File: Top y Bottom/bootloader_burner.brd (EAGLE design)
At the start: 57 x 53.3 mm, 9 parts, among them J1 ZIFSOCKET-28-3", Y1 16MHz

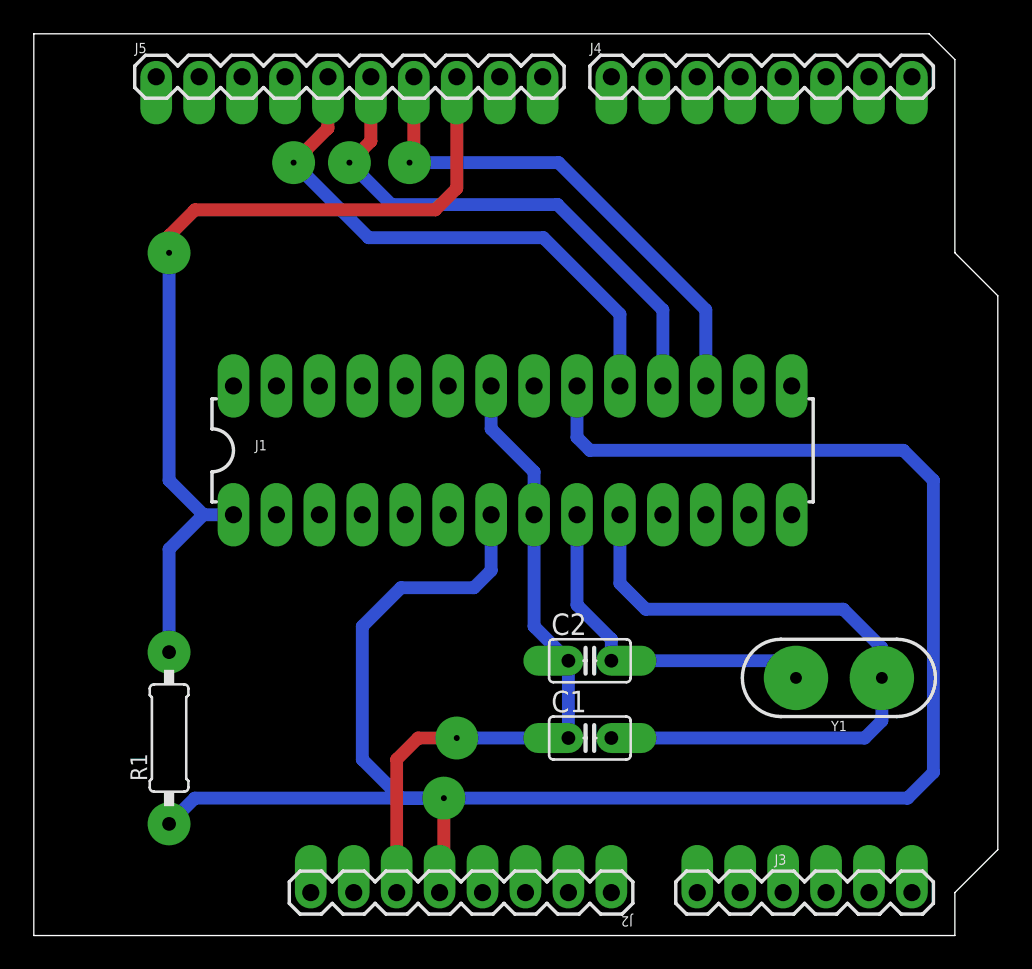
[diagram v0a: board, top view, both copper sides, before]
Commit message: Cambie el diseño de la plaqueta con zif socket grande para que queden ordenados los pines con los del Arduino. Tambien cambie el dieño de la plaqueta doble (que igual hay que cambiarla poque la gracia de esa es que quede montada en el Arduino)
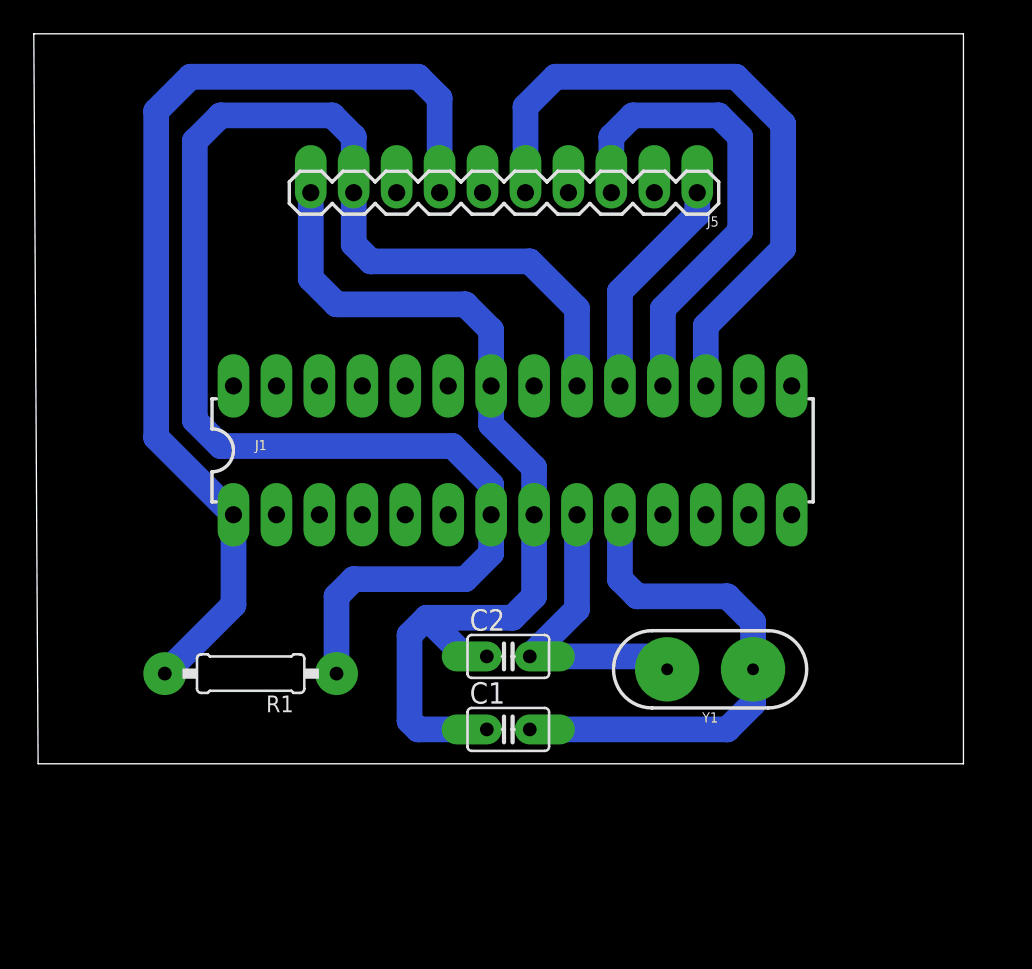
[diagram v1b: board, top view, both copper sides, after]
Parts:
- removed J2, J4: (no value), SparkFun-Connectors:1X08
- removed J3: (no value), SparkFun-Connectors:1X06
- moved J5 32.7 mm to (50.8, 43.9), turned to 180 degrees
- moved Y1 7.64 mm to (51.6, 15.7)
- moved R1 6.15 mm to (24.4, 15.5), turned to 180 degrees
- moved C1 4.85 mm to (39.6, 12.2)
- moved C2 4.83 mm to (39.6, 16.5)
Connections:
- removed net N$1: J1.17, J5.7
- removed net N$2: J1.18, J5.6
- removed net N$3: J1.19, J5.5
- removed net N$6: J1.1, J5.8, R1.2
- new net PIN_10: J1.1, J5.7, R1.2
- new net PIN_11: J1.17, J5.5
- new net PIN_12: J1.18, J5.3
- new net PIN_13: J1.19, J5.1
- net GND: now also J5.10; no longer J2.6
- net VCC: now also J5.9; no longer J2.5
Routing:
- net PIN_10: track 0.00 -> 60.6 mm
- net N$6: track 52.9 -> 0.00 mm, vias 1 -> 0
- net PIN_11: track 0.00 -> 39.6 mm
- net N$3: track 33.2 -> 0.00 mm, vias 1 -> 0
- net N$2: track 32.3 -> 0.00 mm, vias 1 -> 0
- net N$1: track 30.8 -> 0.00 mm, vias 1 -> 0
- net VCC: track 120.6 -> 90.7 mm, vias 1 -> 0
- net PIN_12: track 0.00 -> 28.6 mm
- net GND: track 41.3 -> 56.5 mm, vias 1 -> 0
- net PIN_13: track 0.00 -> 13.3 mm
- net N$5: track 41.9 -> 31.4 mm
- net N$4: track 20.8 -> 18.0 mm
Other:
- board size 57 x 53.3 mm -> 55 x 43.2 mm
